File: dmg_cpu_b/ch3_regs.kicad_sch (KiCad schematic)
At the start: 115 parts

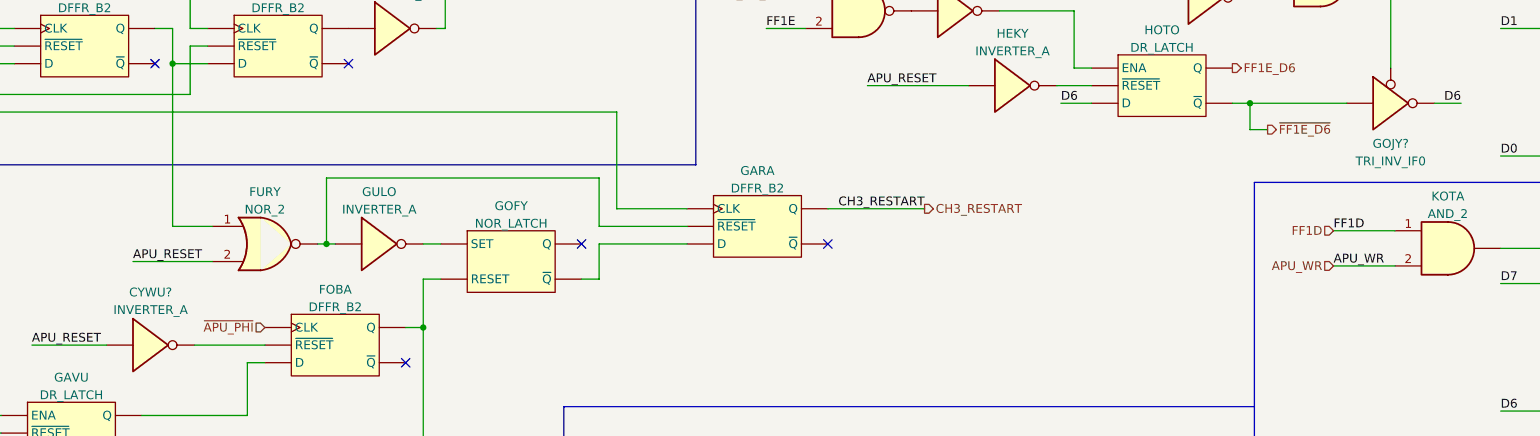
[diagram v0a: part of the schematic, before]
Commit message: fixes made following review
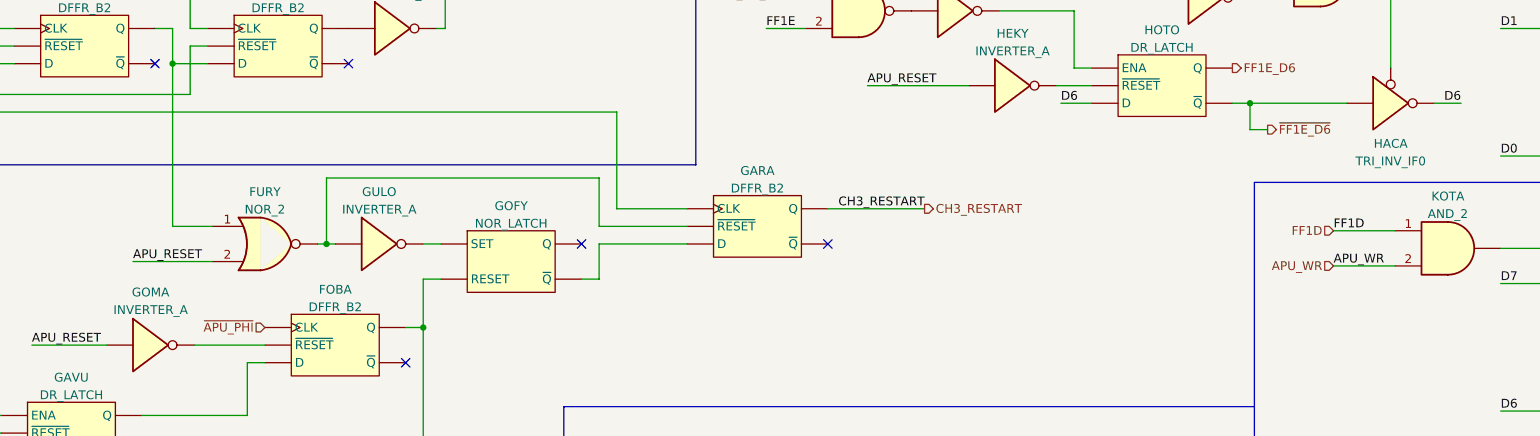
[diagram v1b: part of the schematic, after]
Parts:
- gave numbers to parts that had none: 2
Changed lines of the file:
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@@
   (symbol (lib_id "DMG_CPU_Cells:TRI_INV_IF0") (at 260.985 73.025 0) (unit 1)
     (in_bom yes) (on_board yes) (fields_autoplaced)
-    (property "Reference" "GOJY?" (id 0) (at 260.985 78.8654 0))
+    (property "Reference" "HACA" (id 0) (at 260.985 78.8654 0))
     (property "Value" "TRI_INV_IF0" (id 1) (at 260.985 81.4023 0))
     (property "Footprint" "" (id 2) (at 258.445 73.025 0)
@@
   (symbol (lib_id "DMG_CPU_Cells:INVERTER_A") (at 81.915 107.95 0) (unit 1)
     (in_bom yes) (on_board yes)
-    (property "Reference" "CYWU?" (id 0) (at 81.915 100.33 0))
+    (property "Reference" "GOMA" (id 0) (at 81.915 100.33 0))
     (property "Value" "INVERTER_A" (id 1) (at 81.915 102.87 0))
     (property "Footprint" "" (id 2) (at 79.375 107.95 0)

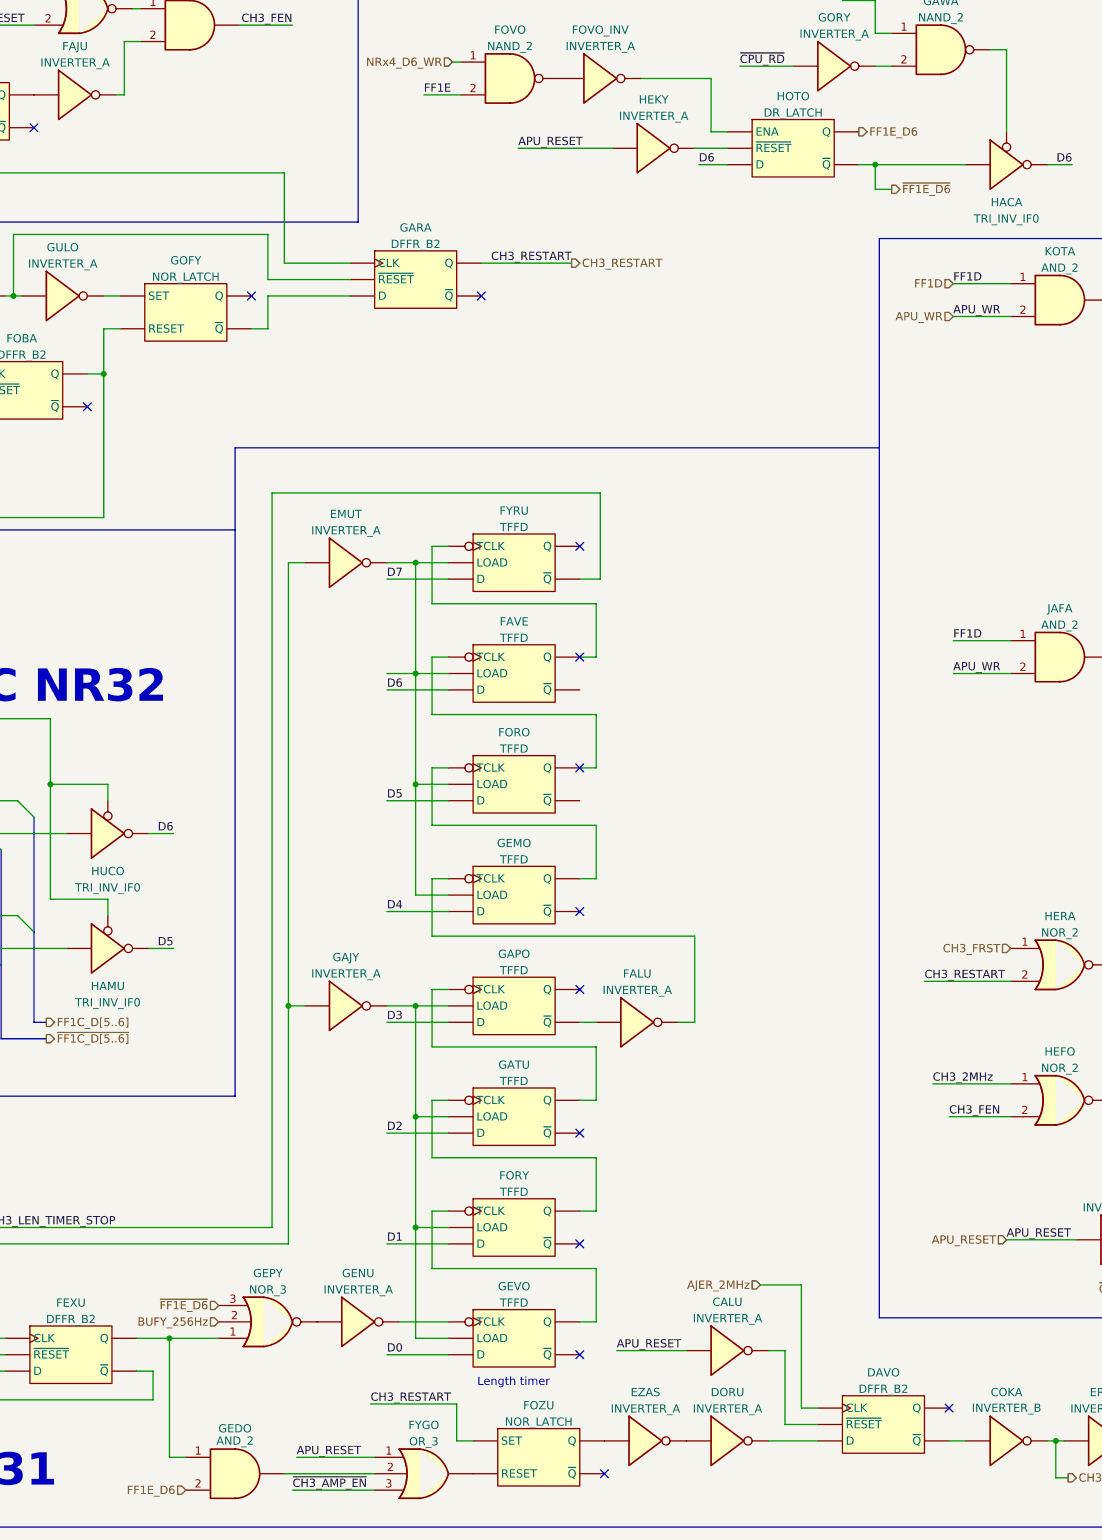
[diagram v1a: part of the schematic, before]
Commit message: Fixes on Data bus page + APU CH4 regs page added.
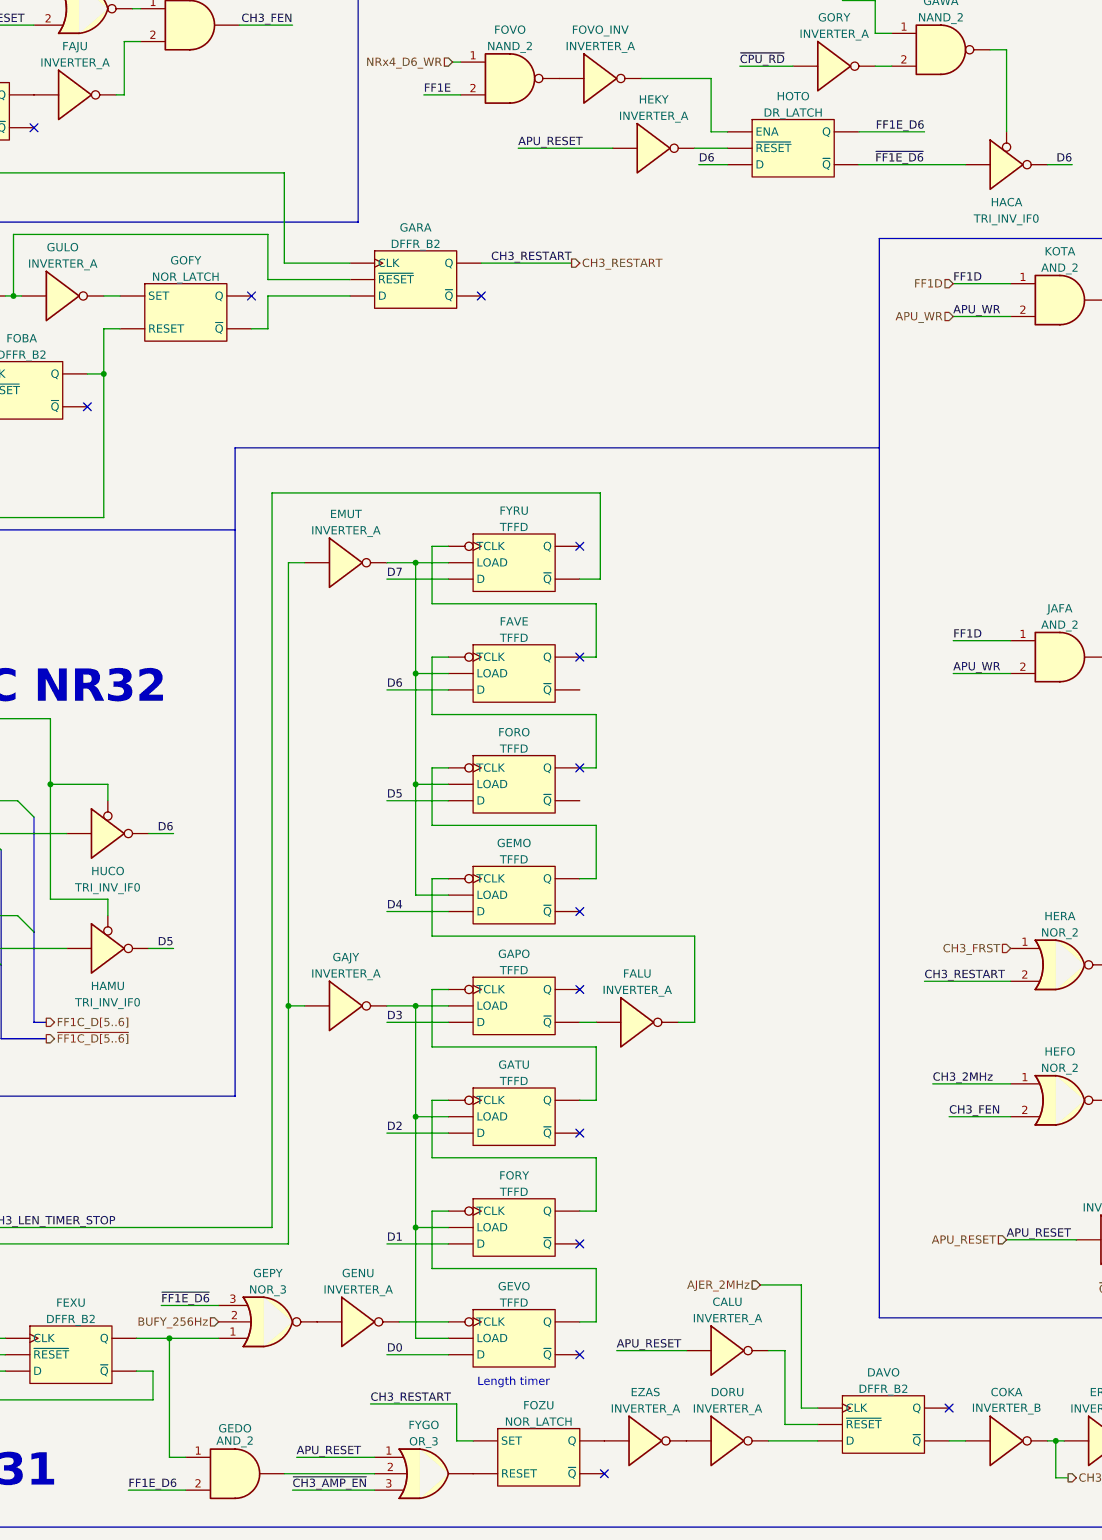
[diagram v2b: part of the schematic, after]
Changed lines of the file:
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@@
   (junction (at 169.545 134.62) (diameter 0) (color 0 0 0 0)
-  )
-  (junction (at 240.665 73.025) (diameter 0) (color 0 0 0 0)
   )
   (junction (at 284.48 186.055) (diameter 0) (color 0 0 0 0)
@@
     (stroke (width 0) (type default) (color 0 0 0 0))
   )
-  (wire (pts (xy 238.125 73.025) (xy 240.665 73.025))
+  (wire (pts (xy 238.125 73.025) (xy 254.635 73.025))
     (stroke (width 0) (type default) (color 0 0 0 0))
   )
@@
     (stroke (width 0) (type default) (color 0 0 0 0))
   )
+  (wire (pts (xy 125.095 278.13) (xy 133.985 278.13))
+    (stroke (width 0) (type default) (color 0 0 0 0))
+  )
   (wire (pts (xy 340.36 36.195) (xy 337.82 36.195))
     (stroke (width 0) (type default) (color 0 0 0 0))
@@
     (stroke (width 0) (type default) (color 0 0 0 0))
   )
-  (wire (pts (xy 240.665 76.835) (xy 240.665 73.025))
-    (stroke (width 0) (type default) (color 0 0 0 0))
-  )
   (wire (pts (xy 59.69 76.835) (xy 59.69 71.755))
     (stroke (width 0) (type default) (color 0 0 0 0))
@@
     (stroke (width 0) (type default) (color 0 0 0 0))
   )
-  (wire (pts (xy 240.665 73.025) (xy 254.635 73.025))
-    (stroke (width 0) (type default) (color 0 0 0 0))
-  )
   (wire (pts (xy 169.545 203.2) (xy 174.625 203.2))
     (stroke (width 0) (type default) (color 0 0 0 0))
@@
     (stroke (width 0) (type default) (color 0 0 0 0))
   )
+  (wire (pts (xy 248.285 67.945) (xy 238.125 67.945))
+    (stroke (width 0) (type default) (color 0 0 0 0))
+  )
   (polyline (pts (xy 13.335 283.845) (xy 298.45 283.845))
     (stroke (width 0) (type default) (color 0 0 0 0))
   )
+  (wire (pts (xy 130.175 249.555) (xy 139.065 249.555))
+    (stroke (width 0) (type default) (color 0 0 0 0))
+  )
   (wire (pts (xy 360.68 199.39) (xy 364.49 199.39))
     (stroke (width 0) (type default) (color 0 0 0 0))
@@
     (stroke (width 0) (type default) (color 0 0 0 0))
   )
-  (wire (pts (xy 165.1 151.765) (xy 169.545 151.765))
-    (stroke (width 0) (type default) (color 0 0 0 0))
-  )
   (wire (pts (xy 287.02 151.765) (xy 289.56 151.765))
     (stroke (width 0) (type default) (color 0 0 0 0))
@@
   )
   (wire (pts (xy 364.49 217.805) (xy 364.49 208.915))
-    (stroke (width 0) (type default) (color 0 0 0 0))
-  )
-  (wire (pts (xy 240.665 76.835) (xy 243.205 76.835))
     (stroke (width 0) (type default) (color 0 0 0 0))
   )
@@
     (effects (font (size 1.27 1.27)) (justify right bottom))
   )
+  (label "~{FF1E_D6}" (at 130.175 249.555 0)
+    (effects (font (size 1.27 1.27)) (justify left bottom))
+  )
   (label "APU_RESET" (at 23.495 118.11 0)
     (effects (font (size 1.27 1.27)) (justify left bottom))
@@
     (effects (font (size 1.27 1.27)) (justify left bottom))
   )
+  (label "FF1E_D6" (at 248.285 67.945 180)
+    (effects (font (size 1.27 1.27)) (justify right bottom))
+  )
   (label "D2" (at 391.16 38.735 180)
     (effects (font (size 1.27 1.27)) (justify right bottom))
@@
     (effects (font (size 1.27 1.27)) (justify left bottom))
   )
+  (label "~{FF1E_D6}" (at 240.665 73.025 0)
+    (effects (font (size 1.27 1.27)) (justify left bottom))
+  )
   (label "FF1E" (at 19.05 112.395 0)
     (effects (font (size 1.27 1.27)) (justify left bottom))
@@
     (effects (font (size 1.27 1.27)) (justify left bottom))
   )
+  (label "FF1E_D6" (at 125.095 278.13 0)
+    (effects (font (size 1.27 1.27)) (justify left bottom))
+  )
   (label "~{CPU_RD}" (at 219.71 57.785 0)
     (effects (font (size 1.27 1.27)) (justify left bottom))
@@
   (label "FF1C" (at 26.67 173.99 0)
     (effects (font (size 1.27 1.27)) (justify left bottom))
-  )
-  (hierarchical_label "~{FF1E_D6}" (shape input) (at 139.065 249.555 180)
-    (effects (font (size 1.27 1.27)) (justify right))
   )
   (hierarchical_label "FF1B" (shape input) (at 55.245 252.73 180)
@@
     (effects (font (size 1.27 1.27)) (justify right))
   )
-  (hierarchical_label "FF1E_D6" (shape input) (at 133.985 278.13 180)
-    (effects (font (size 1.27 1.27)) (justify right))
-  )
   (hierarchical_label "~{APU_PHI}" (shape input) (at 98.425 105.41 180)
     (effects (font (size 1.27 1.27)) (justify right))
   )
-  (hierarchical_label "~{FF1E_D6}" (shape output) (at 243.205 76.835 0)
-    (effects (font (size 1.27 1.27)) (justify left))
-  )
   (hierarchical_label "~{CH3_ACTIVE}" (shape output) (at 282.575 270.51 0)
     (effects (font (size 1.27 1.27)) (justify left))
@@
     (effects (font (size 1.27 1.27)) (justify right))
   )
-  (hierarchical_label "FF1E_D6" (shape output) (at 238.125 67.945 0)
-    (effects (font (size 1.27 1.27)) (justify left))
-  )
   (symbol (lib_id "DMG_CPU_Cells:DFFR_B2") (at 169.545 90.805 0) (unit 1)
